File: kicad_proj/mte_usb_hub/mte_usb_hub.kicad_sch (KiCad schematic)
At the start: 22 parts

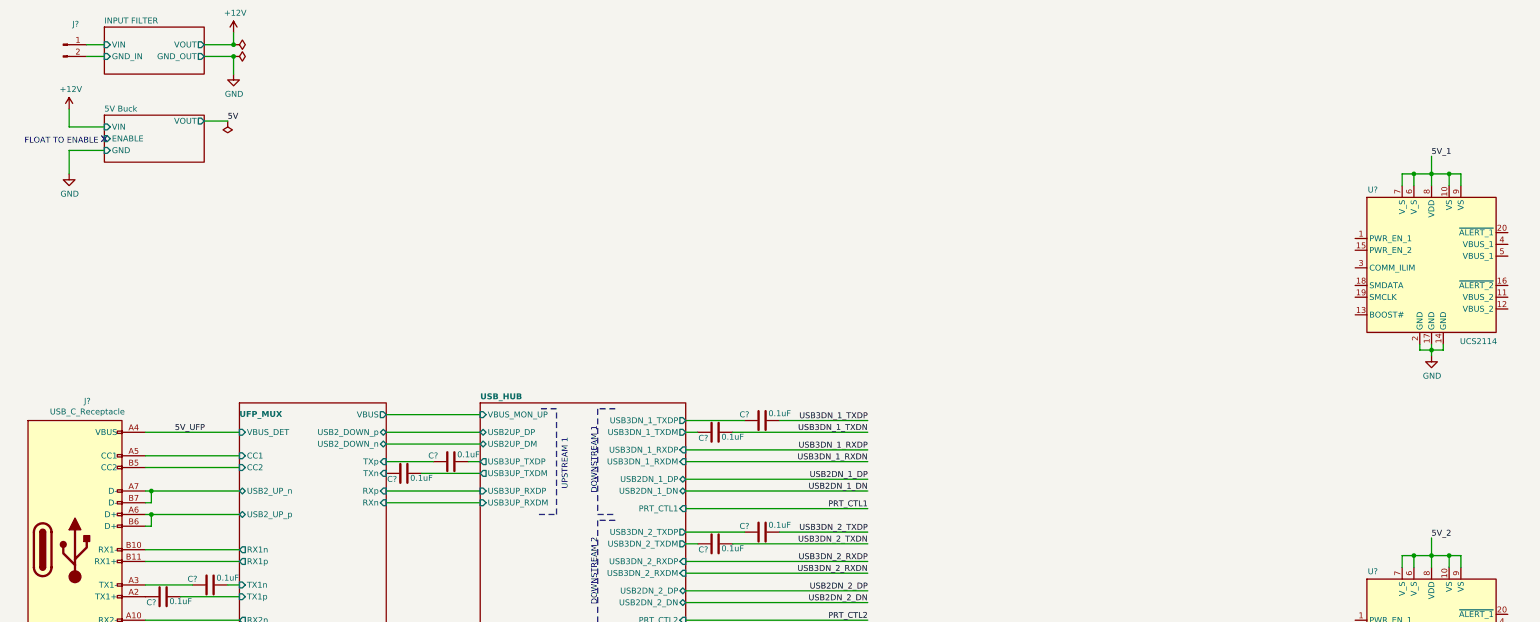
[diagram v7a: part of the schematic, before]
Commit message: Adds 1v15 buck
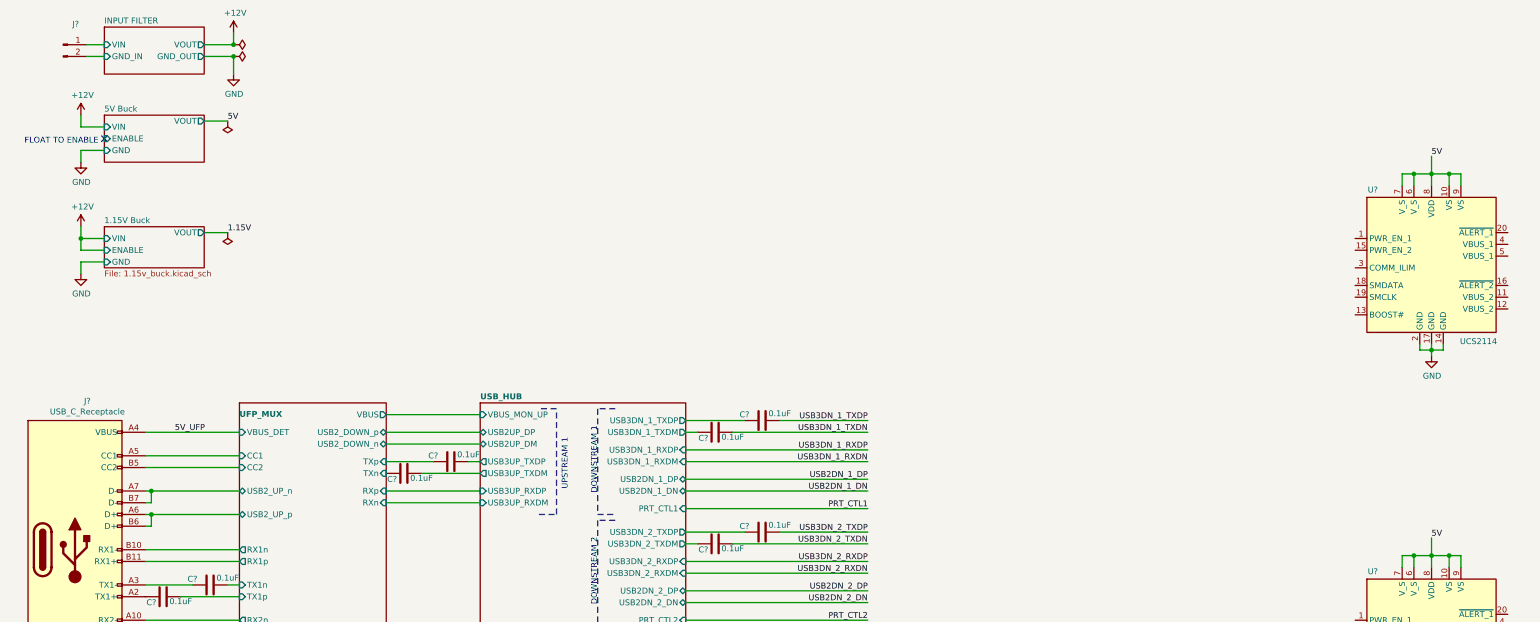
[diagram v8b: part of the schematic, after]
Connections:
- net 5V_1 is gone; now on net 5V: U?.10 (VS), U?.6 (V_S), U?.7 (V_S), U?.8 (VDD), U?.9 (VS)
- net 5V_2 is gone; now on net 5V: U?.10 (VS), U?.6 (V_S), U?.7 (V_S), U?.8 (VDD), U?.9 (VS)
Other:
- added sheet 1.15V Buck (1.15v_buck.kicad_sch)
